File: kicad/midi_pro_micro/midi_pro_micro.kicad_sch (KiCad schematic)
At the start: 4 parts, among them J1 DIN-5_180degree, J2 DIN-5_180degree, U1 ProMicro

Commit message: Draft schematic
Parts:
- removed R1: R_Small, Resistor_SMD:R_0805_2012Metric_Pad1.20x1.40mm_HandSolder, symbol Device:R_Small
- added D1: D, symbol Device:D
- added J4: Conn_01x16_Pin, Connector_PinHeader_2.54mm:PinHeader_1x16_P2.54mm_Vertical, symbol Connector:Conn_01x16_Pin
- added R10, R12, R13, R14, R15, R16, R19, R6, R8: 39k, Resistor_SMD:R_0805_2012Metric_Pad1.20x1.40mm_HandSolder, symbol Device:R_Small
- added R11, R17, R20, R7, R9: 470, Resistor_SMD:R_0805_2012Metric_Pad1.20x1.40mm_HandSolder, symbol Device:R_Small
- added R18: 10k, Resistor_SMD:R_0805_2012Metric_Pad1.20x1.40mm_HandSolder, symbol Device:R_Small
- added R3, R4, R5: 220, Resistor_SMD:R_0805_2012Metric_Pad1.20x1.40mm_HandSolder, symbol Device:R_Small
- added SW1: RotaryEncoder_Switch, Rotary_Encoder:RotaryEncoder_Bourns_Vertical_PEC12R-3x17F-Sxxxx, symbol Device:RotaryEncoder_Switch
- added SW2, SW3, SW4, SW5: SW_Push_LED, lib:SW_PUSH_6mm, symbol Switch:SW_Push_LED
- added U2: AT25xxx, symbol Memory_EEPROM:AT25xxx
- added U3: 6N138, symbol Isolator:6N138
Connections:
- net +5V: now also J4.2 (Pin_2), R10.1, R12.1, R13.1, R14.1, R15.1, R16.1, R17.1, R19.1, R5.2, R6.1, R8.1, U2.8 (VCC), U3.8 (VCC)
- net GND: now also J2.2, J4.1 (Pin_1), R18.2, SW1.C, SW1.S1, SW2.1, SW2.3 (K), SW3.1, SW3.3 (K), SW4.1, SW4.3 (K), SW5.1, SW5.3 (K), U2.4 (GND), U3.5 (GND)
- net at J1.4: now also R3.1
- net at J1.5: now also D1.2 (A), U3.3 (C2)
- net TX: now reaches U1.1 (0,D3,TX)
- net TX: now also R4.1
- net RIGHT_LED: now reaches U1.10 (7,E6)
- net RIGHT_LED: now also R11.2
- net ENC_A: now reaches U1.11 (8,A8,B4)
- net ENC_A: now also R14.2, SW1.A
- net ENC_B: now reaches U1.12 (9,A9,B5)
- net ENC_B: now also R15.2, SW1.B
- net ENC_BTN: now reaches U1.13 (B6,A10,10)
- net ENC_BTN: now also R16.2, SW1.S2
- net MOSI: now reaches U1.14 (B2,16)
- net MOSI: now also J4.14 (Pin_14), U2.5 (MOSI)
- net MISO: now reaches U1.15 (B3,14)
- net MISO: now also J4.13 (Pin_13), U2.2 (MISO)
- net SCK: now reaches U1.16 (B1,15)
- net SCK: now also J4.12 (Pin_12), U2.6 (SCK)
- net OLED_CS: now reaches U1.17 (F7,A0,18)
- net OLED_CS: now also J4.16 (Pin_16)
- net EEPROM_CS: now reaches U1.18 (F6,A1,19)
- net EEPROM_CS: now also U2.1 (~{CS})
- net DOWN_LED: now reaches U1.19 (F5,A2,20)
- net DOWN_LED: now also R20.2
- net RX: now reaches U1.2 (1,D2,RX)
- net RX: now also R17.2, U3.6 (VO2)
- net DOWN_BTN: now reaches U1.20 (F4,A3,21)
- net DOWN_BTN: now also R19.2, SW5.2
- net LEFT_BTN: now reaches U1.5 (2,D1,SDA)
- net LEFT_BTN: now also R8.2, SW3.2
- net LEFT_LED: now reaches U1.6 (3,D0,SCL)
- net LEFT_LED: now also R9.2
- net UP_BTN: now reaches U1.7 (4,A6,D4)
- net UP_BTN: now also R6.2, SW2.2
- net UP_LED: now reaches U1.8 (5,C6)
- net UP_LED: now also R7.2
- net RIGHT_BTN: now reaches U1.9 (6,A7,D7)
- net RIGHT_BTN: now also R10.2, SW4.2
- net at J2.4: now also R5.1
- net at J2.5: now also R4.2
- new net: R11.1, SW4.4 (A)
- new net: R20.1, SW5.4 (A)
- new net: R18.1, U3.7 (VO1)
- new net: D1.1 (K), R3.2, U3.2 (C1)
- new net: R12.2, U2.3 (~{WP})
- new net: R13.2, U2.7 (~{HOLD})
- new net: R7.1, SW2.4 (A)
- new net: R9.1, SW3.4 (A)
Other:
- moved on the sheet: J2

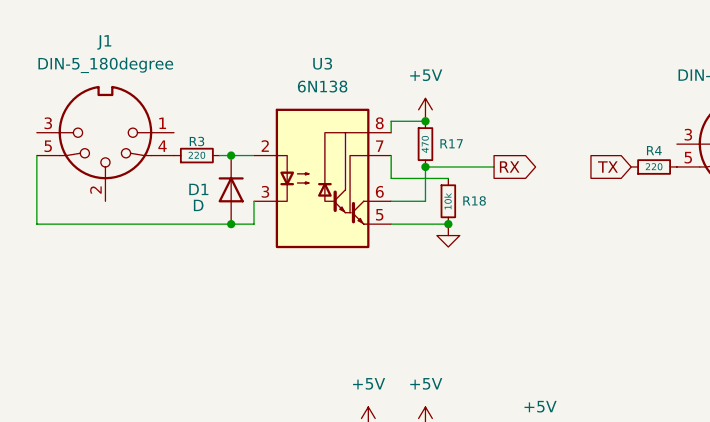
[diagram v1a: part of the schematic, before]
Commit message: Removing MIDI IN
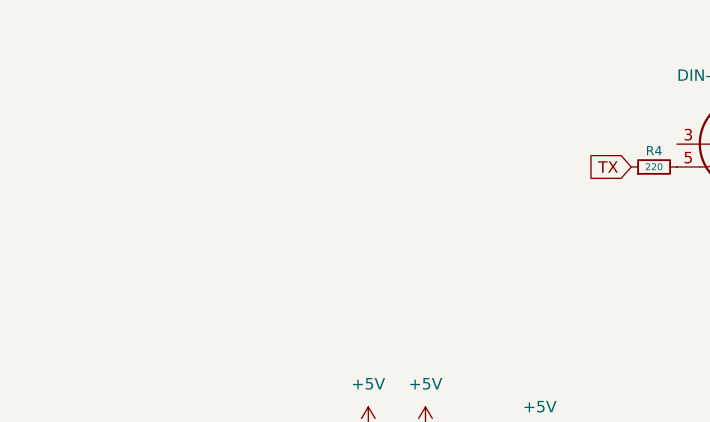
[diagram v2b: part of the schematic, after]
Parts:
- removed D1: D, symbol Device:D
- removed J1: DIN-5_180degree, lib:DIN5MIDI-OOTDTY, symbol Connector:DIN-5_180degree
- removed R17: 470, Resistor_SMD:R_0805_2012Metric_Pad1.20x1.40mm_HandSolder, symbol Device:R_Small
- removed R18: 10k, Resistor_SMD:R_0805_2012Metric_Pad1.20x1.40mm_HandSolder, symbol Device:R_Small
- removed R3: 220, Resistor_SMD:R_0805_2012Metric_Pad1.20x1.40mm_HandSolder, symbol Device:R_Small
- removed U3: 6N138, symbol Isolator:6N138
- SW2, SW3, SW4, SW5: footprint lib:SW_PUSH_6mm -> lib:SW_PUSH_6mm_LED

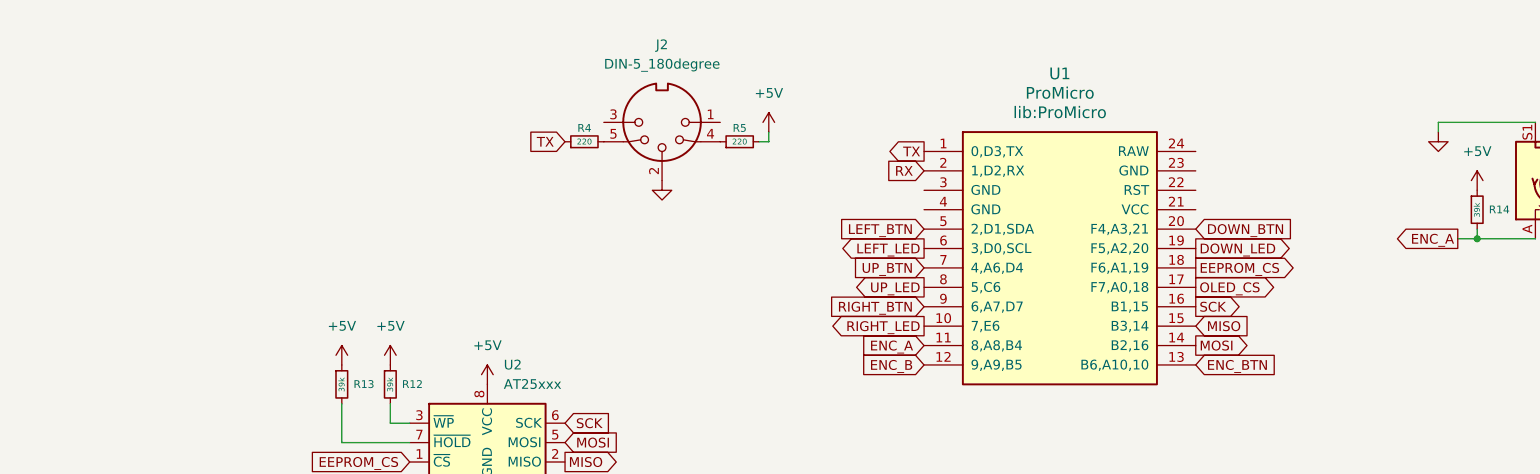
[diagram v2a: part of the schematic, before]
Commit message: Add MIDI IN once again
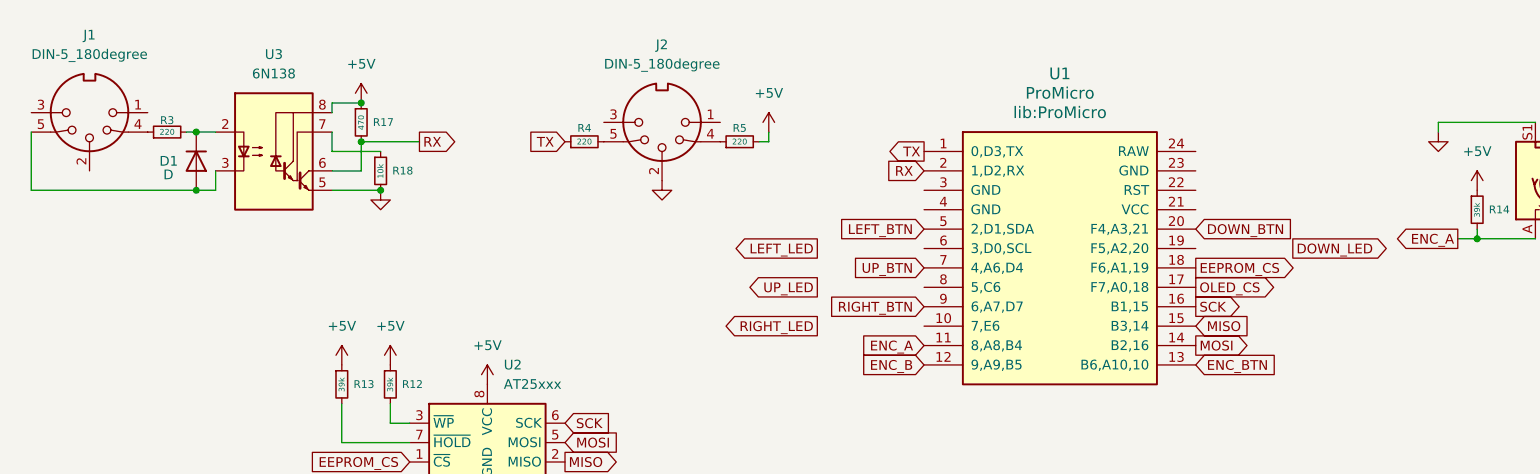
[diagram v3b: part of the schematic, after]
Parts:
- added D1: D, symbol Device:D
- added J1: DIN-5_180degree, lib:DIN5MIDI-OOTDTY, symbol Connector:DIN-5_180degree
- added R17: 470, Resistor_SMD:R_0805_2012Metric_Pad1.20x1.40mm_HandSolder, symbol Device:R_Small
- added R18: 10k, Resistor_SMD:R_0805_2012Metric_Pad1.20x1.40mm_HandSolder, symbol Device:R_Small
- added R3: 220, Resistor_SMD:R_0805_2012Metric_Pad1.20x1.40mm_HandSolder, symbol Device:R_Small
- added U3: 6N138, Package_DIP:DIP-8_W7.62mm_Socket, symbol Isolator:6N138
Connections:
- net +5V: now also R17.1, U3.8 (VCC)
- net DOWN_LED: no longer U1.19 (F5,A2,20)
- net GND: now also R18.2, U3.5 (GND)
- net LEFT_LED: no longer U1.6 (3,D0,SCL)
- net RIGHT_LED: no longer U1.10 (7,E6)
- net RX: now also R17.2, U3.6 (VO2)
- net UP_LED: no longer U1.8 (5,C6)
- new net: J1.4, R3.1
- new net: D1.1 (K), R3.2, U3.2 (C1)
- new net: R18.1, U3.7 (VO1)
- new net: D1.2 (A), J1.5, U3.3 (C2)

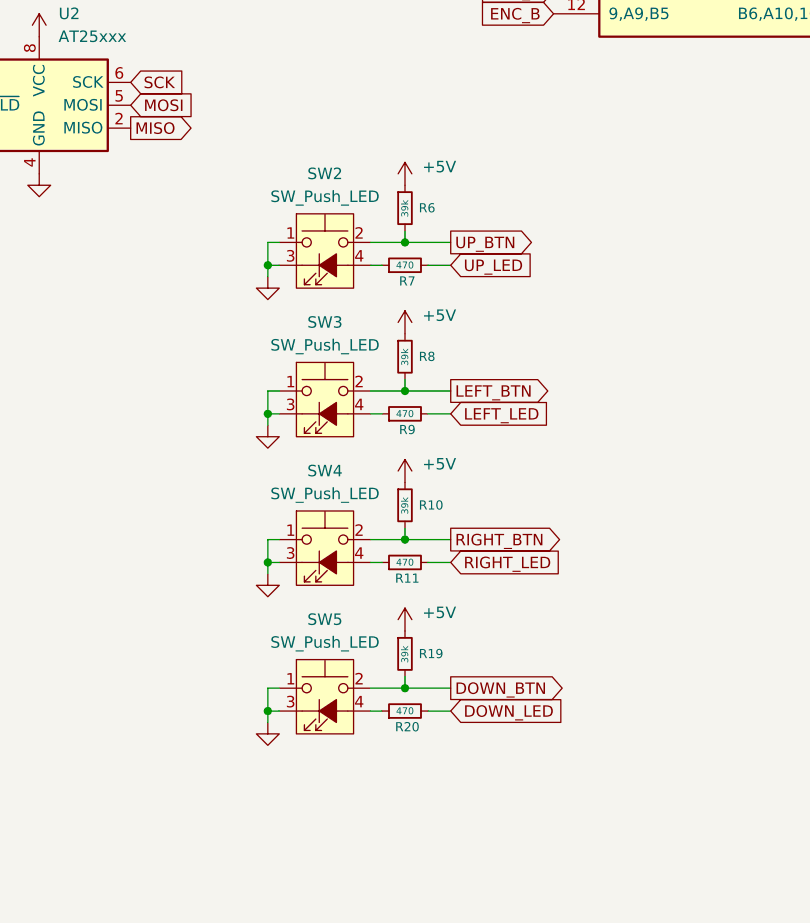
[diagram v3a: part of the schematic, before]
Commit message: Add 5-way button symbol
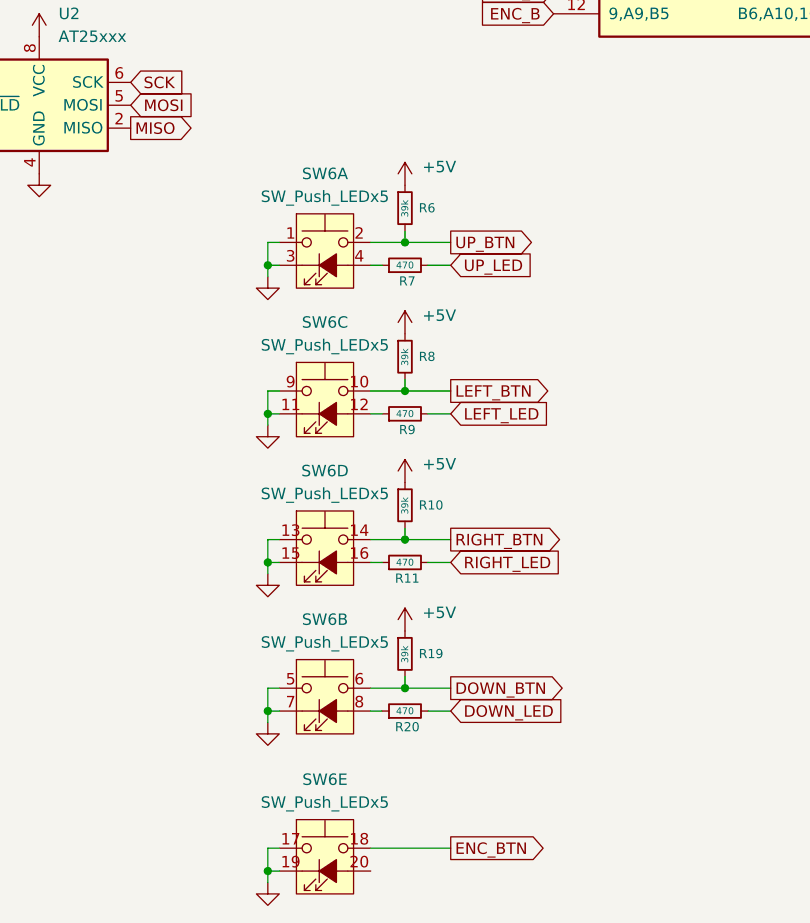
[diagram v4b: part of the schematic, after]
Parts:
- removed SW2, SW3, SW4, SW5: SW_Push_LED, lib:SW_PUSH_6mm_LED, symbol Switch:SW_Push_LED
- added SW6: SW_Push_LEDx5, lib:SW_PUSH_12mm_LEDx5, symbol 5-way-buttons:SW_Push_LEDx5
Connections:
- net DOWN_BTN: now also SW6.6
- net ENC_BTN: now also SW6.18
- net GND: now also SW6.1, SW6.11 (K), SW6.13, SW6.15 (K), SW6.17, SW6.19 (K), SW6.3 (K), SW6.5, SW6.7 (K), SW6.9
- net LEFT_BTN: now also SW6.10
- net RIGHT_BTN: now also SW6.14
- net UP_BTN: now also SW6.2
- net at R11.1: now also SW6.16 (A)
- net at R20.1: now also SW6.8 (A)
- net at R7.1: now also SW6.4 (A)
- net at R9.1: now also SW6.12 (A)

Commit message: 5-way-button board
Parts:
- removed R11, R20, R7, R9: 470, Resistor_SMD:R_0805_2012Metric_Pad1.20x1.40mm_HandSolder, symbol Device:R_Small
- removed SW6: SW_Push_LEDx5, lib:SW_PUSH_12mm_LEDx5, symbol 5-way-buttons:SW_Push_LEDx5
- added J3: Conn_01x12, lib:SW_PUSH_12mm_LEDx5_BOARD, symbol Connector_Generic:Conn_01x12
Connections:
- net DOWN_BTN: now also J3.10 (Pin_10)
- net DOWN_LED: now also J3.11 (Pin_11)
- net GND: now also J3.12 (Pin_12), J3.6 (Pin_6)
- net LEFT_BTN: now also J3.5 (Pin_5)
- net LEFT_LED: now also J3.3 (Pin_3)
- net RIGHT_BTN: now also J3.8 (Pin_8)
- net RIGHT_LED: now also J3.4 (Pin_4)
- net UP_BTN: now also J3.2 (Pin_2)
- net UP_LED: now also J3.1 (Pin_1)
- net ENC_BTN renamed OK_BTN
- net OK_BTN: now also J3.7 (Pin_7)
- new net OK_LED: J3.9 (Pin_9)

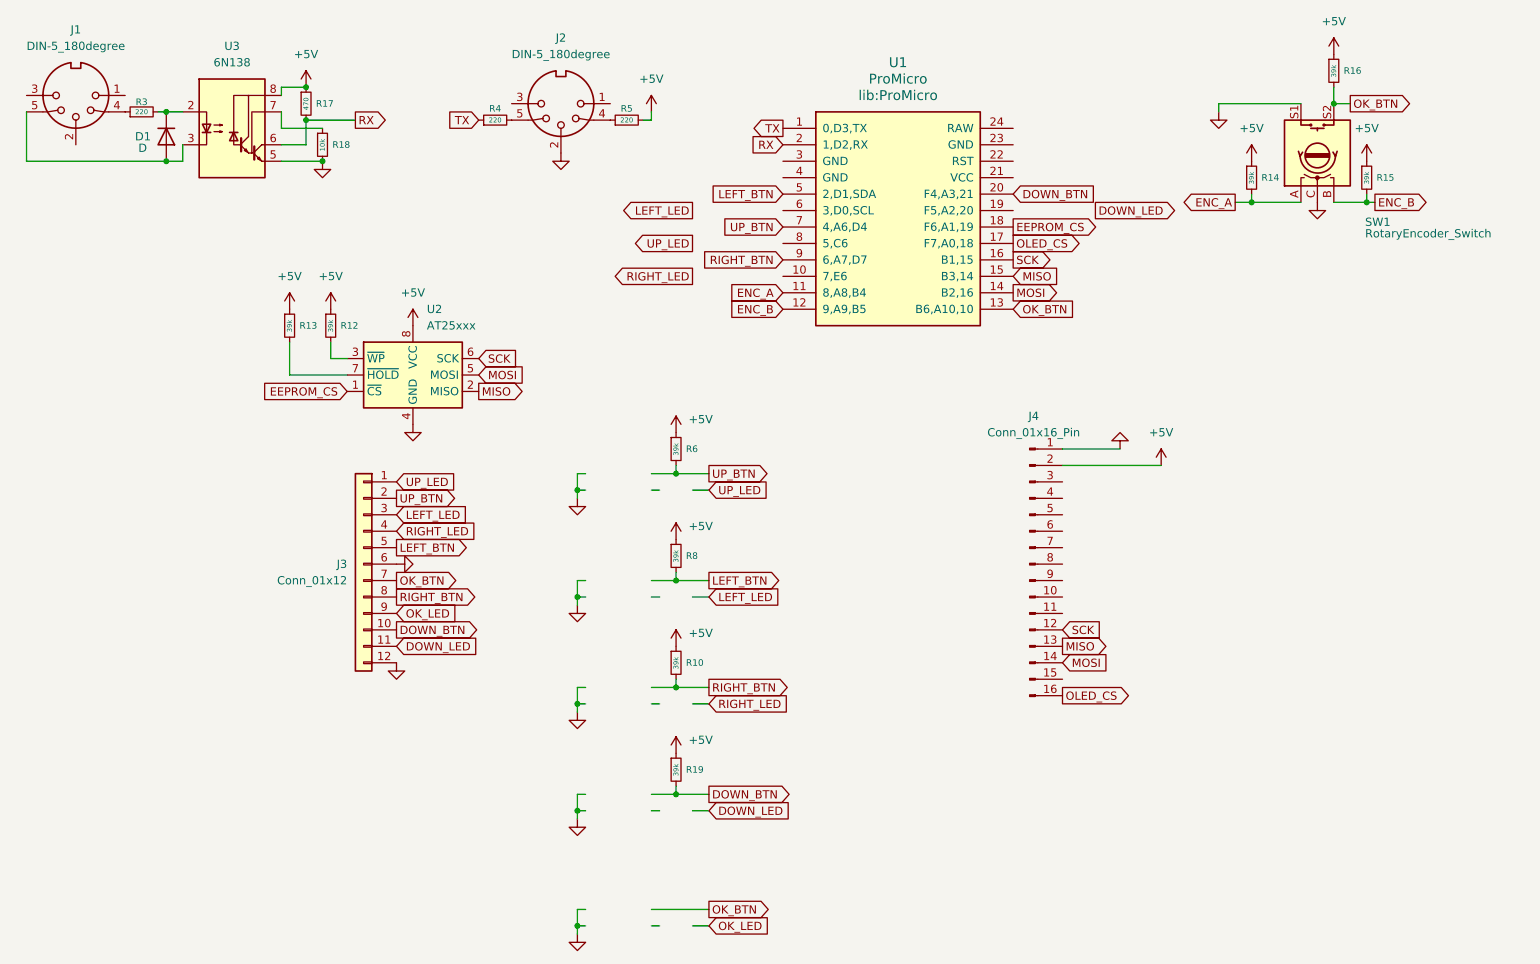
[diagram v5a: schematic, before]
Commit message: Add encoder board
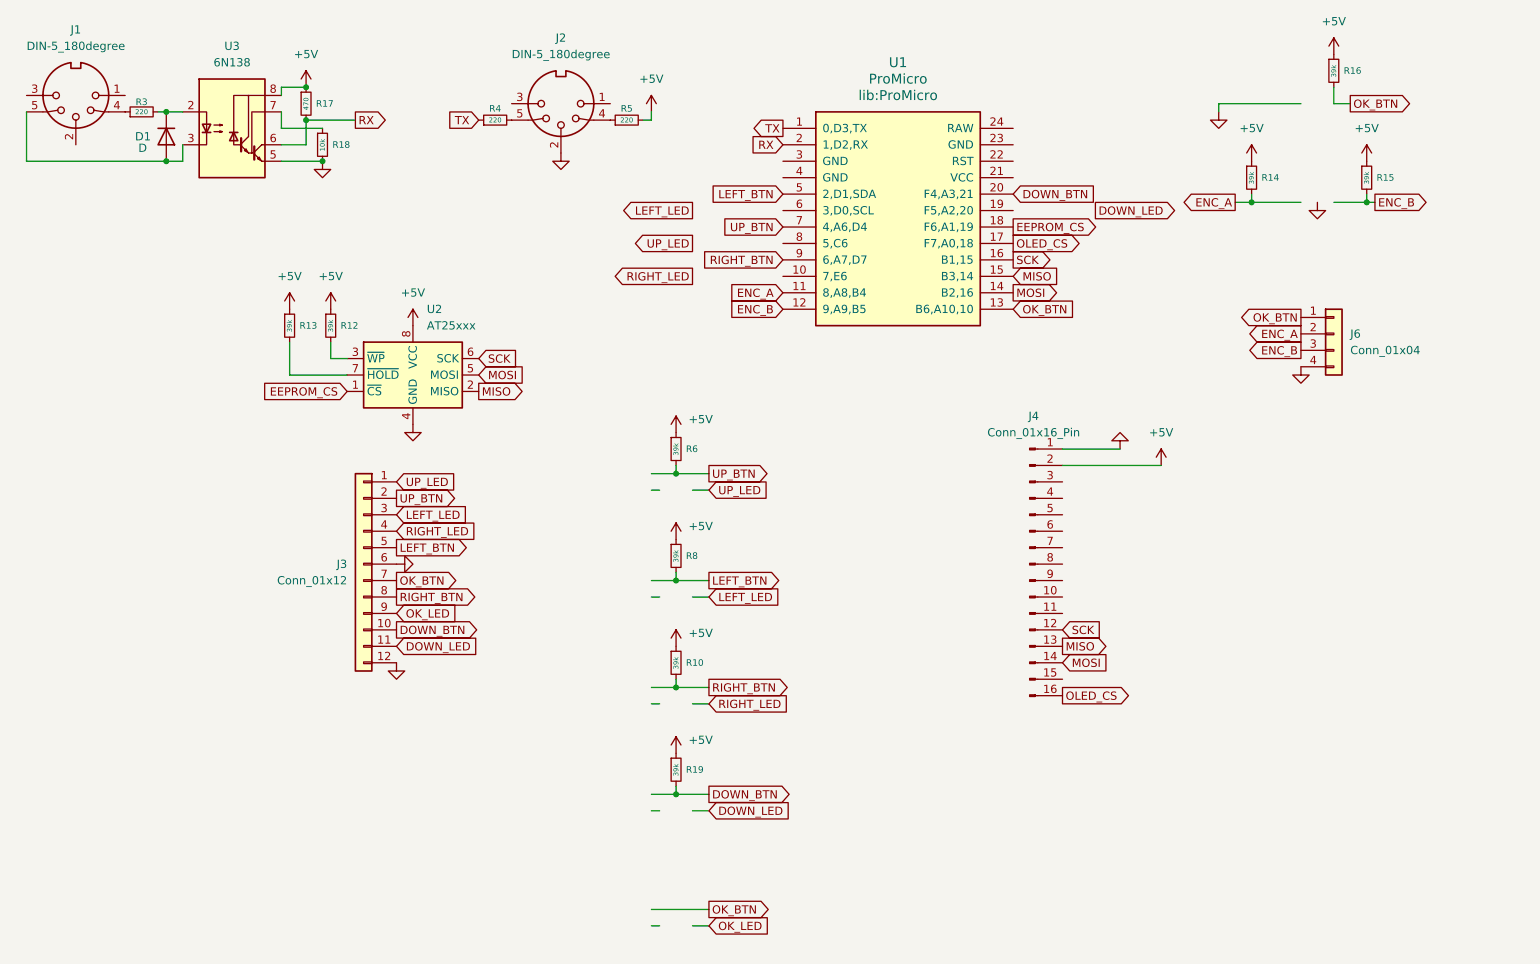
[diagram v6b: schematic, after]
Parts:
- removed SW1: RotaryEncoder_Switch, Rotary_Encoder:RotaryEncoder_Bourns_Vertical_PEC12R-3x17F-Sxxxx, symbol Device:RotaryEncoder_Switch
- added J6: Conn_01x04, lib:Encoder_BOARD-30x40, symbol Connector_Generic:Conn_01x04
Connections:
- net ENC_A: now also J6.2 (Pin_2)
- net ENC_B: now also J6.3 (Pin_3)
- net GND: now also J6.4 (Pin_4)
- net OK_BTN: now also J6.1 (Pin_1)
